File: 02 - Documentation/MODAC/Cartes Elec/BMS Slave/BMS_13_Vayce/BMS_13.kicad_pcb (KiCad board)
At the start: 2 copper layers, 144.5 x 54.5 mm, 112 parts, among them IC1 LT3990EMSE#TRPBF, IC2 LTC6255IS6#TRMPBF, IC3 ADG728BRUZ-REEL7, IC4 ADG728BRUZ-REEL7, J1 Conn_01x02_Pin, J2 Conn_01x07_Pin, J3 Conn_01x02_Pin, J4 Conn_01x08_Pin, J5 Conn_01x08_Pin, J6 Conn_01x07_Pin, Q1 Q_PMOS_GDS, Q10 Q_PMOS_GDS, Q11 Q_PMOS_GDS, Q12 Q_PMOS_GDS, Q18 Q_PMOS_GDS, Q2 Q_PMOS_GDS, Q3 Q_PMOS_GDS, Q4 Q_PMOS_GDS, Q5 Q_PMOS_GDS, Q6 Q_PMOS_GDS, Q7 Q_PMOS_GDS, Q8 Q_PMOS_GDS, Q9 Q_PMOS_GDS, T1 SM91501ALE, U1 ADBMS1818ASWZ

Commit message: BMS 13 0 erreur
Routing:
- net /Cell 12: track 119.2 -> 201.1 mm
- net +BATT: track 208.7 -> 155.5 mm
- net -VDC: track 47.2 -> 82.4 mm, vias 19 -> 22
- net /S6: track 27.3 -> 24.8 mm
- net /S1: track 24.8 -> 22.4 mm
- net /S2: track 24.6 -> 22.2 mm
- net /C6: track 36.6 -> 34.3 mm
- net /S7: track 29.8 -> 27.6 mm
- net /C1: track 32.2 -> 30.1 mm
- net /C7: track 38.5 -> 36.6 mm
- net /S8: track 32.2 -> 30.4 mm
- net /C8: track 41.0 -> 39.4 mm
- net /S9: track 34.7 -> 33.3 mm
- net /C2: track 33.2 -> 31.9 mm
- net /C9: track 43.5 -> 42.2 mm
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
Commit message: J'ai réduit à 17 les avertissements, il ne manque plus que 1 truc de vref que je ne comprends pas et 16 trucs de librairie
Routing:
- net /SCL: track 86.5 -> 85.9 mm
- net Net-(U1-ICMP): vias 3 -> 2
- net -VDC: vias 22 -> 21
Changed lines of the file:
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@@
 		(tags "resistor handsolder")
 		(property "Reference" "R70"
-			(at 0 -1.82 90)
+			(at 0 3 90)
 			(layer "F.SilkS")
 			(effects
@@
 		(tags "SOT TO_SOT_SMD")
 		(property "Reference" "Q11"
-			(at 0 -2.4 180)
+			(at 4.05 -0.05 180)
 			(layer "F.SilkS")
 			(effects
@@
 			(unlocked yes)
 			(layer "F.SilkS")
+			(hide yes)
 			(effects
 				(font
@@
 		(tags "capacitor handsolder")
 		(property "Reference" "C11"
-			(at 0 -1.68 0)
+			(at -0.5375 4.5 0)
 			(layer "F.SilkS")
 			(effects
@@
 		(tags "SOT TO_SOT_SMD")
 		(property "Reference" "Q6"
-			(at 0 -2.4 180)
+			(at 3.4125 0 180)
 			(layer "F.SilkS")
 			(effects
@@
 		(tags "SOT TO_SOT_SMD")
 		(property "Reference" "Q9"
-			(at 0 -2.4 180)
+			(at 3.9125 0.05 180)
 			(layer "F.SilkS")
 			(effects
@@
 		(tags "SOT TO_SOT_SMD")
 		(property "Reference" "Q4"
-			(at 0 -2.4 180)
+			(at 8.05 -1.95 180)
 			(layer "F.SilkS")
 			(effects
@@
 		(tags "SOT TO_SOT_SMD")
 		(property "Reference" "Q3"
-			(at 0 -2.4 180)
+			(at 4.05 0.05 180)
 			(layer "F.SilkS")
 			(effects
@@
 		(tags "MOSFET (P-Channel)")
 		(property "Reference" "Q18"
-			(at -0.013584 -2.730562 0)
+			(at -3.95 1.5 0)
 			(layer "F.SilkS")
 			(effects
 				(font
-					(size 1.27 1.27)
-					(thickness 0.254)
+					(size 1 1)
+					(thickness 0.13)
 				)
 			)
@@
 			(layer "F.Fab")
 		)
-		(fp_text user "${REFERENCE}"
-			(at -5.08 0 0)
-			(layer "F.Fab")
-			(effects
-				(font
-					(size 1.27 1.27)
-					(thickness 0.254)
-				)
-			)
-		)
 		(pad "1" smd rect
 			(at -1.05 -0.95 90)
@@
 		(tags "capacitor handsolder")
 		(property "Reference" "C32"
-			(at 0 -1.68 0)
+			(at 0.5375 3.5 0)
 			(layer "F.SilkS")
 			(effects
@@
 		(tags "capacitor handsolder")
 		(property "Reference" "C6"
-			(at 0 -1.68 90)
+			(at 4.0375 -0.5 90)
 			(layer "F.SilkS")
 			(effects
@@
 		(tags "SOT TO_SOT_SMD")
 		(property "Reference" "Q2"
-			(at 0 -2.4 180)
+			(at 3.55 0 180)
 			(layer "F.SilkS")
 			(effects
@@
 		)
 		(property "Value" "Q_PMOS_GDS"
-			(at 0 2.4 180)
+			(at 8.55 1.5 180)
 			(layer "F.Fab")
 			(effects
@@
 		(tags "SOT TO_SOT_SMD")
 		(property "Reference" "Q5"
-			(at 0 -2.4 180)
+			(at 3.55 0.05 180)
 			(layer "F.SilkS")
 			(effects
@@
 		(tags "SOT TO_SOT_SMD")
 		(property "Reference" "Q7"
-			(at 0 -2.4 180)
+			(at 3.05 0.05 180)
 			(layer "F.SilkS")
 			(effects
@@
 		(tags "SOT TO_SOT_SMD")
 		(property "Reference" "Q10"
-			(at 0 -2.4 180)
+			(at 4.05 0 180)
 			(layer "F.SilkS")
 			(effects
@@
 		(tags "SOT TO_SOT_SMD")
 		(property "Reference" "Q1"
-			(at 0 -2.4 180)
+			(at 6.55 -1 180)
 			(layer "F.SilkS")
 			(effects
@@
 		(tags "SOT TO_SOT_SMD")
 		(property "Reference" "Q8"
-			(at 0 -2.4 180)
+			(at 3.55 0 180)
 			(layer "F.SilkS")
 			(effects
@@
 		)
 	)
-	(gr_text "-V\n"
-		(at 175.5 102.5 0)
-		(layer "F.SilkS")
-		(effects
-			(font
-				(size 1 1)
-				(thickness 0.15)
-			)
-			(justify bottom)
-		)
-	)
 	(gr_text "T9"
 		(at 177.563923 80.285286 0)
@@
 	)
 	(via
-		(at 178 74.5)
-		(size 0.7)
-		(drill 0.4)
-		(layers "F.Cu" "B.Cu")
-		(free yes)
-		(net 6)
-	)
-	(via
 		(at 131 69.5)
 		(size 0.7)
@@
 	)
 	(segment
-		(start 135.396576 96.75)
-		(end 135.323288 96.676712)
-		(width 0.3)
-		(layer "F.Cu")
-		(net 21)
-	)
-	(segment
 		(start 127 74.5)
 		(end 127 73.5375)
@@
 	)
 	(segment
-		(start 135.5 77)
-		(end 135.25 77.25)
-		(width 0.25)
-		(layer "B.Cu")
-		(net 26)
-	)
-	(segment
 		(start 133.5 79)
 		(end 135.5 77)
@@
 	)
 	(segment
-		(start 184.564592 82.225)
-		(end 184.919796 82.580204)
-		(width 0.3)
-		(layer "B.Cu")
-		(net 37)
-	)
-	(segment
 		(start 159.5 103)
 		(end 159.5 114.5)
@@
 	)
 	(segment
-		(start 138.348592 97.651408)
-		(end 136.285788 95.588604)
-		(width 0.25)
-		(layer "F.Cu")
-		(net 55)
-	)
-	(segment
 		(start 139 97)
 		(end 140.5 97)
@@
 	)
 	(segment
+		(start 138.348592 97.580698)
+		(end 135.075 94.307106)
+		(width 0.25)
+		(layer "F.Cu")
+		(net 55)
+	)
+	(segment
 		(start 141.999999 101)
 		(end 141.999999 100.037199)
@@
 	)
 	(segment
-		(start 136.285788 95.517894)
-		(end 136 95.232106)
-		(width 0.25)
-		(layer "F.Cu")
-		(net 55)
-	)
-	(segment
-		(start 136.017894 95.25)
-		(end 136 95.232106)
-		(width 0.3)
-		(layer "F.Cu")
-		(net 55)
-	)
-	(segment
 		(start 135.075 94.307106)
 		(end 135.075 77.826472)
@@
 	)
 	(segment
-		(start 136 95.232106)
-		(end 135.075 94.307106)
-		(width 0.3)
+		(start 138.348592 97.651408)
+		(end 138.348592 97.580698)
+		(width 0.25)
 		(layer "F.Cu")
 		(net 55)
@@
 		(net 55)
 	)
-	(segment
-		(start 136.285788 95.588604)
-		(end 136.285788 95.517894)
-		(width 0.25)
-		(layer "F.Cu")
-		(net 55)
-	)
 	(via
 		(at 158.5 106.5)
@@
 	)
 	(segment
-		(start 135.18947 97.25)
-		(end 135 97.06053)
-		(width 0.3)
-		(layer "F.Cu")
-		(net 57)
-	)
-	(segment
 		(start 133.075 81.951472)
 		(end 127.623528 76.5)
@@
 	)
 	(segment
-		(start 134.775258 98.25)
-		(end 134.762629 98.237371)
-		(width 0.3)
-		(layer "F.Cu")
-		(net 58)
-	)
-	(segment
 		(start 132.075 84.951472)
 		(end 127.623528 80.5)
@@
 	)
 	(segment
-		(start 133.969864 100.27303)
-		(end 133.946834 100.25)
-		(width 0.25)
-		(layer "F.Cu")
-		(net 60)
-	)
-	(segment
 		(start 130.075 96.378166)
 		(end 130.075 90.951472)
@@
 	)
 	(segment
-		(start 134 100.303166)
-		(end 133.946834 100.25)
-		(width 0.25)
-		(layer "F.Cu")
-		(net 60)
-	)
-	(segment
 		(start 133.969864 103.241236)
 		(end 133.969864 100.27303)
@@
 	)
 	(segment
-		(start 133 100.717378)
-		(end 132.891311 100.608689)
-		(width 0.25)
-		(layer "F.Cu")
-		(net 61)
-	)
-	(segment
 		(start 129.075 96.792378)
 		(end 129.075 93.951472)
@@
 	)
 	(segment
-		(start 133.068198 100.785576)
-		(end 133 100.717378)
-		(width 0.25)
-		(layer "F.Cu")
-		(net 61)
-	)
-	(segment
 		(start 127.623528 92.5)
 		(end 124.55 92.5)
@@
 	)
 	(segment
-		(start 144.499999 112.3538)
-		(end 144.499999 113.5)
-		(width 0.25)
-		(layer "F.Cu")
-		(net 67)
-	)
-	(segment
-		(start 144.5 113.5)
-		(end 144.499999 113.5)
+		(start 144.5 114.5)
+		(end 144.5 112.353801)
 		(width 0.25)
 		(layer "F.Cu")
@@
 	)
 	(segment
-		(start 144.499999 113.5)
-		(end 144.499999 114.499999)
+		(start 144.5 112.353801)
+		(end 144.499999 112.3538)
 		(width 0.25)
 		(layer "F.Cu")
@@
 	)
 	(segment
-		(start 161.519748 93.519748)
-		(end 161.5 93.5)
-		(width 0.3)
-		(layer "F.Cu")
-		(net 68)
-	)
-	(segment
 		(start 160.325 98.825)
 		(end 160.5 99)
@@
 	)
 	(segment
-		(start 117.45 64.5)
-		(end 117.5 64.5)
-		(width 0.3)
-		(layer "F.Cu")
-		(net 72)
-	)
-	(segment
 		(start 115.5 64)
 		(end 117 64)
@@
 		(size 0.8)
 		(drill 0.4)
-		(layers "F.Cu" "B.Cu")
-		(net 122)
-	)
-	(via
-		(at 154 103)
-		(size 0.8)
-		(drill 0.4)

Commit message: bien_relié
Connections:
- C11 pad 2: Net-(U1-VREF2) -> /VREF2
- U1 pad 50: Net-(U1-VREF2) -> /VREF2
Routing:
- net /VREF2: track 24.4 -> 54.0 mm, vias 2 -> 4
- net Net-(U1-VREF2): track 13.5 -> 0.00 mm

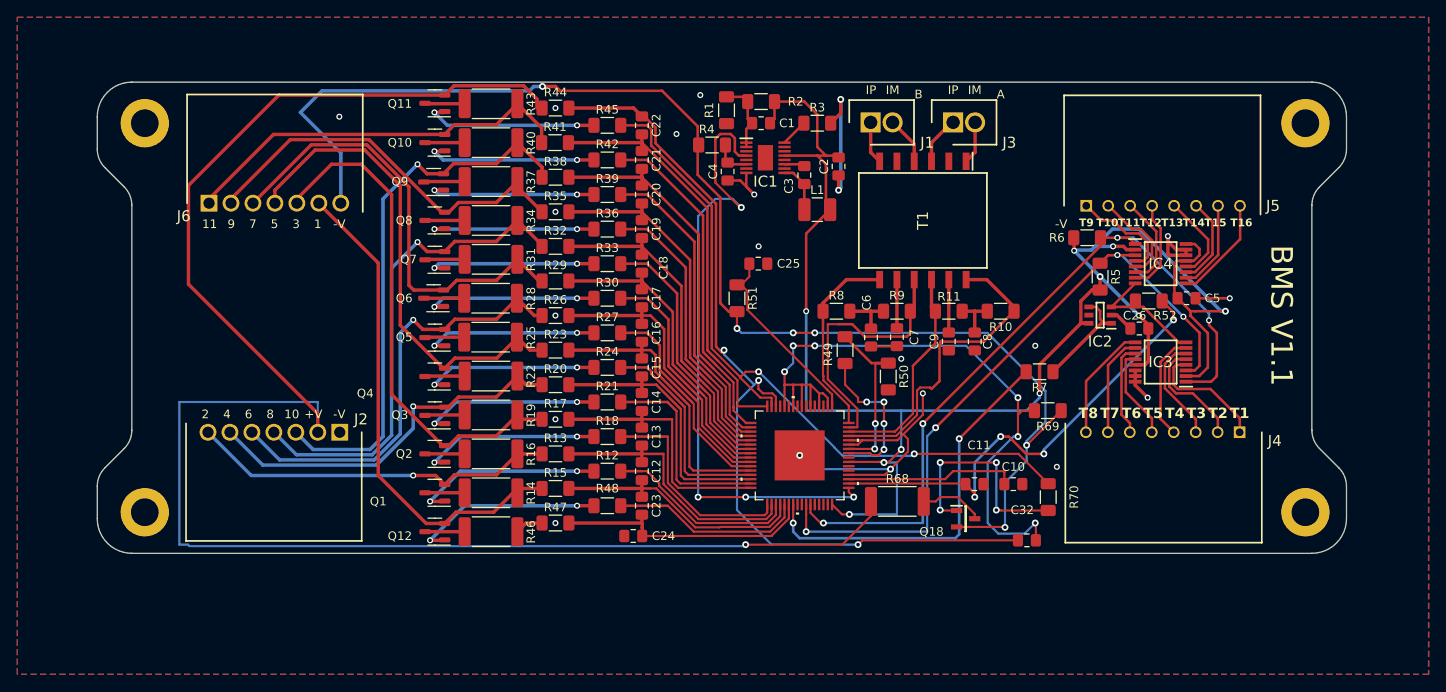
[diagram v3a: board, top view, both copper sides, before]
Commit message: Modif bms13
Déplacement et autres
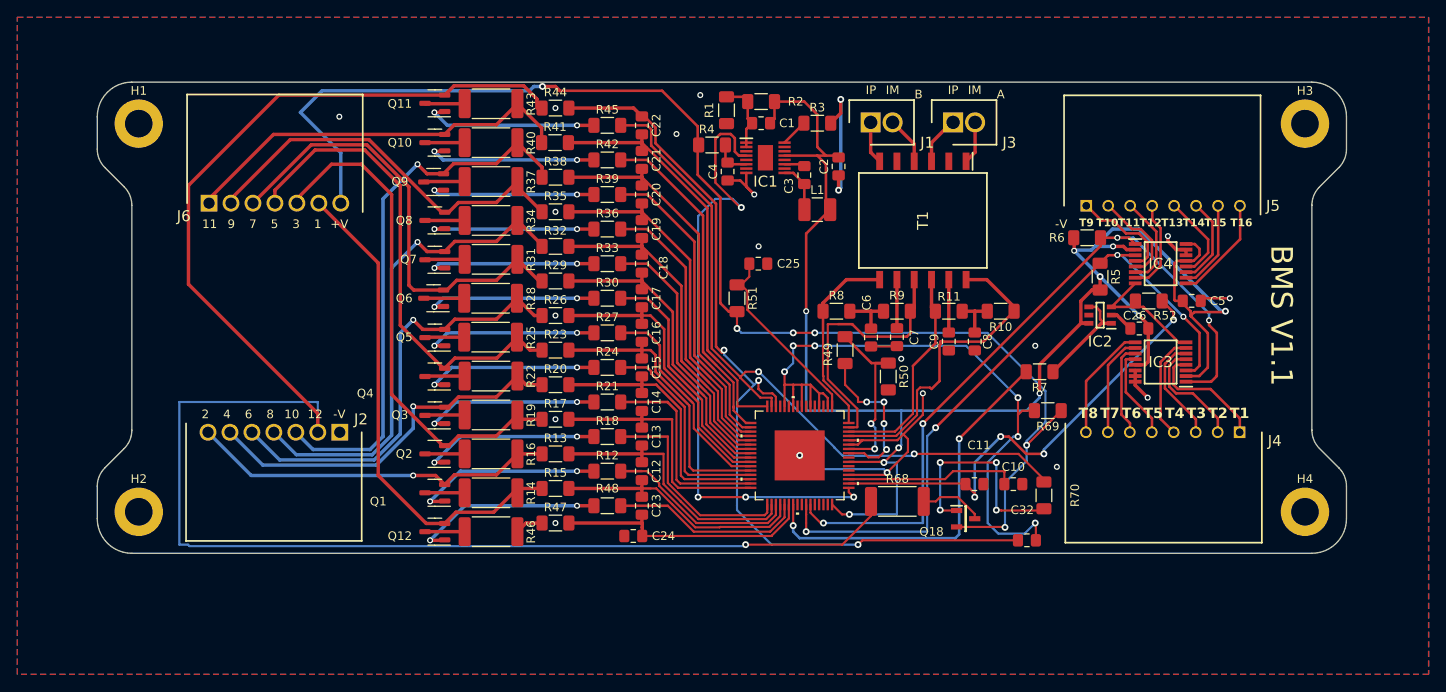
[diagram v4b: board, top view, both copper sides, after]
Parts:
- removed ? (x3): , 
- removed REF**: MountingHole_3.2mm_M3_DIN965_Pad, MountingHole:MountingHole_3.2mm_M3_DIN965_Pad
- added H1: MountingHole, MountingHole:MountingHole_3.2mm_M3_DIN965_Pad, F.Cu at (68.8, 68.3)
- added H2: MountingHole, MountingHole:MountingHole_3.2mm_M3_DIN965_Pad, F.Cu at (68.8, 113.2)
- added H3: MountingHole, MountingHole:MountingHole_3.2mm_M3_DIN965_Pad, F.Cu at (203.7, 68.3)
- added H4: MountingHole, MountingHole:MountingHole_3.2mm_M3_DIN965_Pad, F.Cu at (203.7, 113.2)
- moved C5 0.67 mm to (190.6, 88.8)
- moved R70 0.54 mm to (173.5, 111.3)
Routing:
- net -VDC: track 82.4 -> 77.5 mm
- net +5V: track 197.8 -> 198.7 mm
- net Net-(U1-IBIAS): track 18.0 -> 18.6 mm
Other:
- board text added: "12"

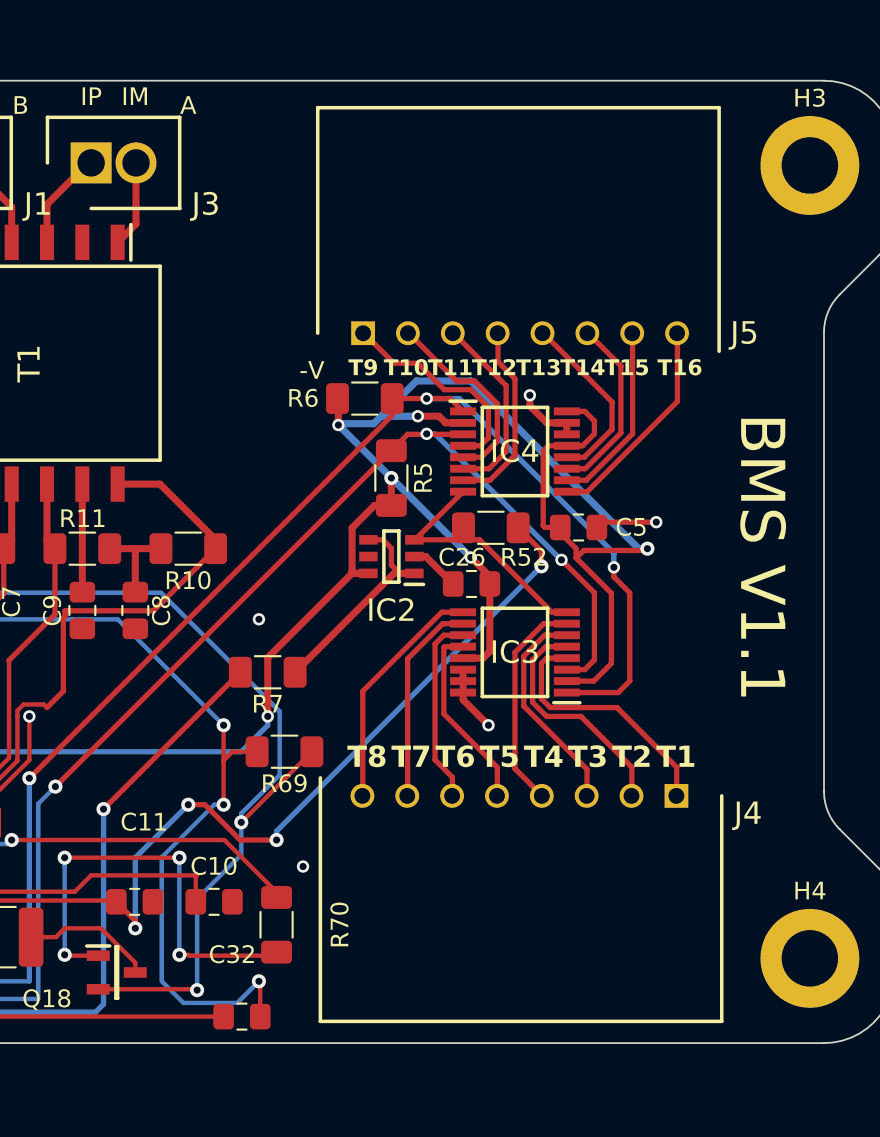
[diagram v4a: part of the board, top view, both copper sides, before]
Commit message: Ajout du VDC-  aux connecteurs BMS + fichiers de prod + TS Schematic update
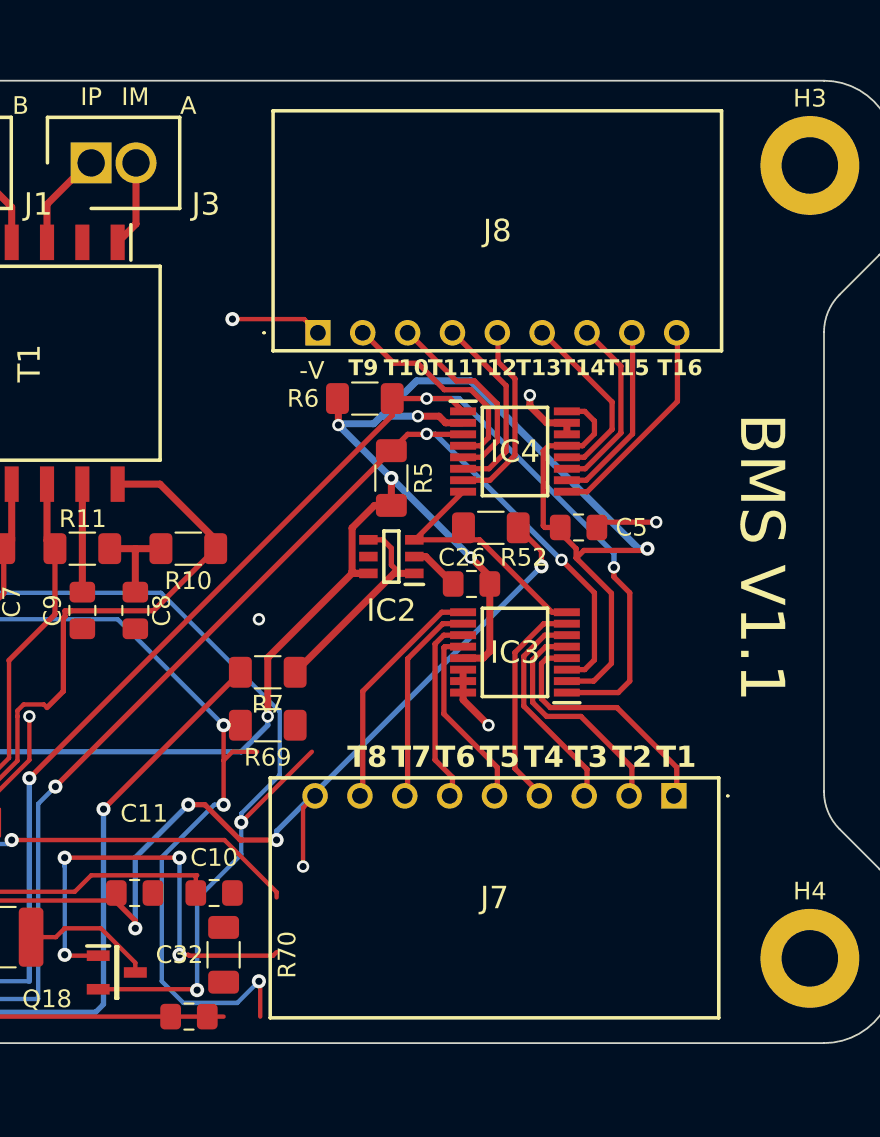
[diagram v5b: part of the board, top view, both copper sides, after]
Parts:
- removed J4, J5: Conn_01x08_Pin, EPSA_lib:SHDRRA8W50P0X254_1X8_2273X1359X741P
- added J7: Conn_01x09_Pin, 5-1049359:51049359, F.Cu at (196.0, 104.0)
- added J8: Conn_01x09_Pin, 5-1049359:51049359, F.Cu at (175.8, 77.8)
- moved R70 3.45 mm to (170.5, 113.0)
- moved C32 3.00 mm to (168.5, 116.5)
- moved R69 1.78 mm to (173.0, 100.0)
- moved C10 0.50 mm to (170.0, 109.5)
- moved C11 0.50 mm to (165.5, 109.5)
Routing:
- net /T9: track 12.2 -> 17.3 mm, vias 0 -> 1
- net -VDC: track 77.5 -> 81.8 mm

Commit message: Restauration version Axel de février 2025
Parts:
- removed J7, J8: Conn_01x09_Pin, 5-1049359:51049359
- added J4: Conn_01x08_Pin, EPSA_lib:SHDRRA8W50P0X254_1X8_2273X1359X741P, F.Cu at (196.1, 104.0)
- added J5: Conn_01x08_Pin, EPSA_lib:SHDRRA8W50P0X254_1X8_2273X1359X741P, F.Cu at (178.4, 77.8)
- moved R70 3.45 mm to (173.5, 111.3)
- moved C32 3.00 mm to (171.5, 116.5)
- moved R69 1.78 mm to (173.9, 101.5)
- moved C10 0.50 mm to (170.0, 110.0)
- moved C11 0.50 mm to (165.5, 110.0)
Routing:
- net /T9: track 17.3 -> 12.2 mm, vias 1 -> 0
- net -VDC: track 81.8 -> 77.5 mm
